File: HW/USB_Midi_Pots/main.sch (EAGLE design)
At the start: 61 parts, among them SW1 EC12E_SW

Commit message: HW update
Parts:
- added C20: (no value), Ai_Passives:CAP0805
- added USB2: (no value), pinhead:PINHD-1X4
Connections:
- net +5V: now also C20.1, USB2.4
- net GND: now also C20.2, USB2.1
- net N$1: now also USB2.3
- net N$2: now also USB2.2
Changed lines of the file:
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@@
 <setting verticaltext="up"/>
 </settings>
-<grid distance="0.05" unitdist="inch" unit="inch" style="lines" multiple="1" display="no" altdistance="0.01" altunitdist="inch" altunit="inch"/>
+<grid distance="0.1" unitdist="inch" unit="inch" style="lines" multiple="1" display="no" altdistance="0.01" altunitdist="inch" altunit="inch"/>
 <layers>
 <layer number="1" name="Top" color="4" fill="1" visible="no" active="no"/>
@@
 <layer number="113" name="IDFDebug" color="4" fill="1" visible="yes" active="yes"/>
 <layer number="116" name="Patch_BOT" color="9" fill="4" visible="no" active="yes"/>
+<layer number="117" name="mPads" color="7" fill="1" visible="no" active="no"/>
+<layer number="118" name="mVias" color="7" fill="1" visible="no" active="no"/>
+<layer number="119" name="mUnrouted" color="7" fill="1" visible="no" active="no"/>
+<layer number="120" name="mDimension" color="7" fill="1" visible="no" active="no"/>
 <layer number="121" name="_tsilk" color="7" fill="1" visible="no" active="yes"/>
 <layer number="122" name="_bsilk" color="7" fill="1" visible="no" active="yes"/>
@@
 <layer number="127" name="_tValues" color="7" fill="1" visible="yes" active="yes"/>
 <layer number="128" name="_bValues" color="7" fill="1" visible="yes" active="yes"/>
+<layer number="129" name="mtStop" color="7" fill="1" visible="no" active="no"/>
+<layer number="130" name="mbStop" color="7" fill="1" visible="no" active="no"/>
 <layer number="131" name="tAdjust" color="7" fill="1" visible="no" active="yes"/>
 <layer number="132" name="bAdjust" color="7" fill="1" visible="no" active="yes"/>
+<layer number="133" name="mtFinish" color="7" fill="1" visible="no" active="no"/>
+<layer number="134" name="mbFinish" color="7" fill="1" visible="no" active="no"/>
+<layer number="135" name="mtGlue" color="7" fill="1" visible="no" active="no"/>
+<layer number="136" name="mbGlue" color="7" fill="1" visible="no" active="no"/>
+<layer number="137" name="mtTest" color="7" fill="1" visible="no" active="no"/>
+<layer number="138" name="mbTest" color="7" fill="1" visible="no" active="no"/>
+<layer number="139" name="mtKeepout" color="7" fill="1" visible="no" active="no"/>
+<layer number="140" name="mbKeepout" color="7" fill="1" visible="no" active="no"/>
+<layer number="141" name="mtRestrict" color="7" fill="1" visible="no" active="no"/>
+<layer number="142" name="mbRestrict" color="7" fill="1" visible="no" active="no"/>
+<layer number="143" name="mvRestrict" color="7" fill="1" visible="no" active="no"/>
 <layer number="144" name="Drill_legend" color="7" fill="1" visible="no" active="yes"/>
+<layer number="145" name="mHoles" color="7" fill="1" visible="no" active="no"/>
+<layer number="146" name="mMilling" color="7" fill="1" visible="no" active="no"/>
+<layer number="147" name="mMeasures" color="7" fill="1" visible="no" active="no"/>
+<layer number="148" name="mDocument" color="7" fill="1" visible="no" active="no"/>
+<layer number="149" name="mReference" color="7" fill="1" visible="no" active="no"/>
 <layer number="150" name="Notes" color="7" fill="1" visible="no" active="yes"/>
 <layer number="151" name="HeatSink" color="7" fill="1" visible="no" active="yes"/>
@@
 <layer number="154" name="FabDoc2" color="2" fill="1" visible="no" active="no"/>
 <layer number="155" name="FabDoc3" color="7" fill="15" visible="no" active="no"/>
+<layer number="191" name="mNets" color="7" fill="1" visible="no" active="no"/>
+<layer number="192" name="mBusses" color="7" fill="1" visible="no" active="no"/>
+<layer number="193" name="mPins" color="7" fill="1" visible="no" active="no"/>
+<layer number="194" name="mSymbols" color="7" fill="1" visible="no" active="no"/>
+<layer number="195" name="mNames" color="7" fill="1" visible="no" active="no"/>
+<layer number="196" name="mValues" color="7" fill="1" visible="no" active="no"/>
 <layer number="199" name="Contour" color="7" fill="1" visible="no" active="yes"/>
 <layer number="200" name="200bmp" color="1" fill="10" visible="no" active="yes"/>
@@
 <part name="P+11" library="supply1" library_urn="urn:adsk.eagle:library:371" deviceset="+5V" device=""/>
 <part name="GND17" library="supply1" library_urn="urn:adsk.eagle:library:371" deviceset="GND" device=""/>
+<part name="C20" library="Ai_Passives" deviceset="CAP" device="0805"/>
+<part name="USB2" library="pinhead" library_urn="urn:adsk.eagle:library:325" deviceset="PINHD-1X4" device="" package3d_urn="urn:adsk.eagle:package:22407/2"/>
 </parts>
 <sheets>
@@
 <instance part="P+11" gate="1" x="110.49" y="33.02" rot="R90"/>
 <instance part="GND17" gate="1" x="110.49" y="40.64" rot="R270"/>
+<instance part="C20" gate="G$1" x="-5.08" y="233.68"/>
+<instance part="USB2" gate="A" x="-88.9" y="96.52" rot="R180"/>
 </instances>
 <busses>
@@
 <pinref part="C5" gate="G$1" pin="2"/>
 <wire x1="-12.7" y1="226.06" x2="-12.7" y2="228.6" width="0.1524" layer="91"/>
+<pinref part="C20" gate="G$1" pin="2"/>
+<wire x1="-5.08" y1="228.6" x2="-5.08" y2="226.06" width="0.1524" layer="91"/>
+<wire x1="-5.08" y1="226.06" x2="-12.7" y2="226.06" width="0.1524" layer="91"/>
+<junction x="-12.7" y="226.06"/>
 </segment>
 <segment>
@@
 <wire x1="-86.36" y1="38.1" x2="-83.82" y2="38.1" width="0.1524" layer="91"/>
 <junction x="-83.82" y="38.1"/>
+<wire x1="-68.58" y1="72.39" x2="-68.58" y2="71.12" width="0.1524" layer="91"/>
+<junction x="-68.58" y="48.26"/>
+<pinref part="USB2" gate="A" pin="1"/>
+<wire x1="-68.58" y1="71.12" x2="-68.58" y2="48.26" width="0.1524" layer="91"/>
+<wire x1="-86.36" y1="91.44" x2="-71.12" y2="91.44" width="0.1524" layer="91"/>
+<wire x1="-71.12" y1="91.44" x2="-68.58" y2="91.44" width="0.1524" layer="91"/>
+<wire x1="-68.58" y1="91.44" x2="-68.58" y2="71.12" width="0.1524" layer="91"/>
 </segment>
 <segment>
@@
 <wire x1="12.7" y1="50.8" x2="-21.59" y2="50.8" width="0.1524" layer="91"/>
 <wire x1="-21.59" y1="50.8" x2="-21.59" y2="58.42" width="0.1524" layer="91"/>
-<wire x1="-21.59" y1="58.42" x2="-73.66" y2="58.42" width="0.1524" layer="91"/>
+<wire x1="-21.59" y1="58.42" x2="-60.96" y2="58.42" width="0.1524" layer="91"/>
 <pinref part="P+5" gate="1" pin="+5V"/>
+<wire x1="-60.96" y1="58.42" x2="-73.66" y2="58.42" width="0.1524" layer="91"/>
 <wire x1="12.7" y1="53.34" x2="12.7" y2="50.8" width="0.1524" layer="91"/>
 <junction x="12.7" y="50.8"/>
 <pinref part="U$2" gate="G$1" pin="VCC"/>
+<wire x1="-60.96" y1="80.01" x2="-60.96" y2="78.74" width="0.1524" layer="91"/>
+<wire x1="-60.96" y1="78.74" x2="-60.96" y2="58.42" width="0.1524" layer="91"/>
+<junction x="-60.96" y="58.42"/>
+<pinref part="USB2" gate="A" pin="4"/>
+<wire x1="-86.36" y1="99.06" x2="-60.96" y2="99.06" width="0.1524" layer="91"/>
+<wire x1="-60.96" y1="99.06" x2="-60.96" y2="96.52" width="0.1524" layer="91"/>
+<wire x1="-60.96" y1="96.52" x2="-60.96" y2="78.74" width="0.1524" layer="91"/>
 </segment>
 <segment>
@@
 <wire x1="-20.32" y1="238.76" x2="-20.32" y2="241.3" width="0.1524" layer="91"/>
 <junction x="-20.32" y="241.3"/>
+<pinref part="C20" gate="G$1" pin="1"/>
+<wire x1="-5.08" y1="238.76" x2="-5.08" y2="241.3" width="0.1524" layer="91"/>
+<wire x1="-5.08" y1="241.3" x2="-12.7" y2="241.3" width="0.1524" layer="91"/>
+<junction x="-12.7" y="241.3"/>
 </segment>
 <segment>
@@
 <wire x1="-45.72" y1="46.99" x2="-45.72" y2="55.88" width="0.1524" layer="91"/>
 <junction x="-45.72" y="55.88"/>
-<wire x1="-73.66" y1="55.88" x2="-45.72" y2="55.88" width="0.1524" layer="91"/>
+<wire x1="-73.66" y1="55.88" x2="-63.5" y2="55.88" width="0.1524" layer="91"/>
 <pinref part="U$2" gate="G$1" pin="D-"/>
+<wire x1="-63.5" y1="55.88" x2="-45.72" y2="55.88" width="0.1524" layer="91"/>
+<wire x1="-63.5" y1="77.47" x2="-63.5" y2="76.2" width="0.1524" layer="91"/>
+<wire x1="-63.5" y1="76.2" x2="-63.5" y2="55.88" width="0.1524" layer="91"/>
+<junction x="-63.5" y="55.88"/>
+<pinref part="USB2" gate="A" pin="3"/>
+<wire x1="-86.36" y1="96.52" x2="-63.5" y2="96.52" width="0.1524" layer="91"/>
+<wire x1="-63.5" y1="96.52" x2="-63.5" y2="76.2" width="0.1524" layer="91"/>
 </segment>
 </net>
@@
 <wire x1="-40.64" y1="46.99" x2="-40.64" y2="53.34" width="0.1524" layer="91"/>
 <junction x="-40.64" y="53.34"/>
-<wire x1="-73.66" y1="53.34" x2="-40.64" y2="53.34" width="0.1524" layer="91"/>
+<wire x1="-73.66" y1="53.34" x2="-66.04" y2="53.34" width="0.1524" layer="91"/>
 <pinref part="U$2" gate="G$1" pin="D+"/>
+<wire x1="-66.04" y1="53.34" x2="-40.64" y2="53.34" width="0.1524" layer="91"/>
+<wire x1="-66.04" y1="74.93" x2="-66.04" y2="73.66" width="0.1524" layer="91"/>
+<wire x1="-66.04" y1="73.66" x2="-66.04" y2="53.34" width="0.1524" layer="91"/>
+<junction x="-66.04" y="53.34"/>
+<pinref part="USB2" gate="A" pin="2"/>
+<wire x1="-86.36" y1="93.98" x2="-66.04" y2="93.98" width="0.1524" layer="91"/>
+<wire x1="-66.04" y1="93.98" x2="-66.04" y2="73.66" width="0.1524" layer="91"/>
 </segment>
 </net>

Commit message: Board Update
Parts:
- added D7: (no value), Ai_LED:LED0603
- added L3: (no value), Ai_Passives:IND0603
- added R6: (no value), Ai_Passives:RES0603
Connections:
- new net N$36: R6.1, U$1.(INT6/AIN0)PE6
- new net N$38: D7.A, R6.2
- new net N$40: L3.1, U$2.VCC, USB2.4
- net +5V: now also L3.2; no longer U$2.VCC, USB2.4
- net GND: now also D7.C
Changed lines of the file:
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@@
 <setting verticaltext="up"/>
 </settings>
-<grid distance="0.1" unitdist="inch" unit="inch" style="lines" multiple="1" display="no" altdistance="0.01" altunitdist="inch" altunit="inch"/>
+<grid distance="0.05" unitdist="inch" unit="inch" style="lines" multiple="1" display="no" altdistance="0.01" altunitdist="inch" altunit="inch"/>
 <layers>
 <layer number="1" name="Top" color="4" fill="1" visible="no" active="no"/>
@@
 <part name="C20" library="Ai_Passives" deviceset="CAP" device="0805"/>
 <part name="USB2" library="pinhead" library_urn="urn:adsk.eagle:library:325" deviceset="PINHD-1X4" device="" package3d_urn="urn:adsk.eagle:package:22407/2"/>
+<part name="R6" library="Ai_Passives" deviceset="RES" device="0603"/>
+<part name="D7" library="Ai_LED" deviceset="LED" device="0603"/>
+<part name="L3" library="Ai_Passives" deviceset="IND" device="0603"/>
 </parts>
 <sheets>
@@
 <instance part="C20" gate="G$1" x="-5.08" y="233.68"/>
 <instance part="USB2" gate="A" x="-88.9" y="96.52" rot="R180"/>
+<instance part="R6" gate="G$1" x="92.71" y="58.42"/>
+<instance part="D7" gate="G$1" x="109.22" y="58.42" rot="R90"/>
+<instance part="L3" gate="G$1" x="-7.62" y="50.8" rot="R90"/>
 </instances>
 <busses>
@@
 <junction x="118.11" y="71.12"/>
 <pinref part="PIN8" gate="G$1" pin="C"/>
-<wire x1="114.3" y1="66.04" x2="118.11" y2="66.04" width="0.1524" layer="91"/>
+<wire x1="114.3" y1="66.04" x2="116.84" y2="66.04" width="0.1524" layer="91"/>
+<wire x1="116.84" y1="66.04" x2="118.11" y2="66.04" width="0.1524" layer="91"/>
 <wire x1="118.11" y1="66.04" x2="118.11" y2="68.58" width="0.1524" layer="91"/>
 <pinref part="PIN7" gate="G$1" pin="C"/>
@@
 <wire x1="107.95" y1="68.58" x2="118.11" y2="68.58" width="0.1524" layer="91"/>
 <junction x="118.11" y="68.58"/>
+<pinref part="D7" gate="G$1" pin="C"/>
+<wire x1="114.3" y1="58.42" x2="116.84" y2="58.42" width="0.1524" layer="91"/>
+<wire x1="116.84" y1="58.42" x2="116.84" y2="66.04" width="0.1524" layer="91"/>
+<junction x="116.84" y="66.04"/>
 </segment>
 <segment>
@@
 <wire x1="21.59" y1="60.96" x2="21.59" y2="50.8" width="0.1524" layer="91"/>
 <wire x1="21.59" y1="50.8" x2="12.7" y2="50.8" width="0.1524" layer="91"/>
-<wire x1="12.7" y1="50.8" x2="-21.59" y2="50.8" width="0.1524" layer="91"/>
-<wire x1="-21.59" y1="50.8" x2="-21.59" y2="58.42" width="0.1524" layer="91"/>
-<wire x1="-21.59" y1="58.42" x2="-60.96" y2="58.42" width="0.1524" layer="91"/>
 <pinref part="P+5" gate="1" pin="+5V"/>
-<wire x1="-60.96" y1="58.42" x2="-73.66" y2="58.42" width="0.1524" layer="91"/>
 <wire x1="12.7" y1="53.34" x2="12.7" y2="50.8" width="0.1524" layer="91"/>
+<pinref part="L3" gate="G$1" pin="2"/>
+<wire x1="-2.54" y1="50.8" x2="12.7" y2="50.8" width="0.1524" layer="91"/>
 <junction x="12.7" y="50.8"/>
-<pinref part="U$2" gate="G$1" pin="VCC"/>
-<wire x1="-60.96" y1="80.01" x2="-60.96" y2="78.74" width="0.1524" layer="91"/>
-<wire x1="-60.96" y1="78.74" x2="-60.96" y2="58.42" width="0.1524" layer="91"/>
-<junction x="-60.96" y="58.42"/>
-<pinref part="USB2" gate="A" pin="4"/>
-<wire x1="-86.36" y1="99.06" x2="-60.96" y2="99.06" width="0.1524" layer="91"/>
-<wire x1="-60.96" y1="99.06" x2="-60.96" y2="96.52" width="0.1524" layer="91"/>
-<wire x1="-60.96" y1="96.52" x2="-60.96" y2="78.74" width="0.1524" layer="91"/>
 </segment>
 <segment>
@@
 </segment>
 </net>
+<net name="N$36" class="0">
+<segment>
+<pinref part="U$1" gate="G$1" pin="(INT6/AIN0)PE6"/>
+<pinref part="R6" gate="G$1" pin="1"/>
+<wire x1="83.82" y1="58.42" x2="87.63" y2="58.42" width="0.1524" layer="91"/>
+</segment>
+</net>
+<net name="N$38" class="0">
+<segment>
+<pinref part="R6" gate="G$1" pin="2"/>
+<pinref part="D7" gate="G$1" pin="A"/>
+<wire x1="97.79" y1="58.42" x2="106.68" y2="58.42" width="0.1524" layer="91"/>
+</segment>
+</net>
+<net name="N$40" class="0">
+<segment>
+<pinref part="L3" gate="G$1" pin="1"/>
+<wire x1="-21.59" y1="50.8" x2="-12.7" y2="50.8" width="0.1524" layer="91"/>
+<wire x1="-21.59" y1="50.8" x2="-21.59" y2="58.42" width="0.1524" layer="91"/>
+<wire x1="-21.59" y1="58.42" x2="-60.96" y2="58.42" width="0.1524" layer="91"/>
+<wire x1="-60.96" y1="58.42" x2="-73.66" y2="58.42" width="0.1524" layer="91"/>
+<pinref part="U$2" gate="G$1" pin="VCC"/>
+<wire x1="-60.96" y1="99.06" x2="-60.96" y2="58.42" width="0.1524" layer="91"/>
+<junction x="-60.96" y="58.42"/>
+<pinref part="USB2" gate="A" pin="4"/>
+<wire x1="-86.36" y1="99.06" x2="-60.96" y2="99.06" width="0.1524" layer="91"/>
+</segment>
+</net>

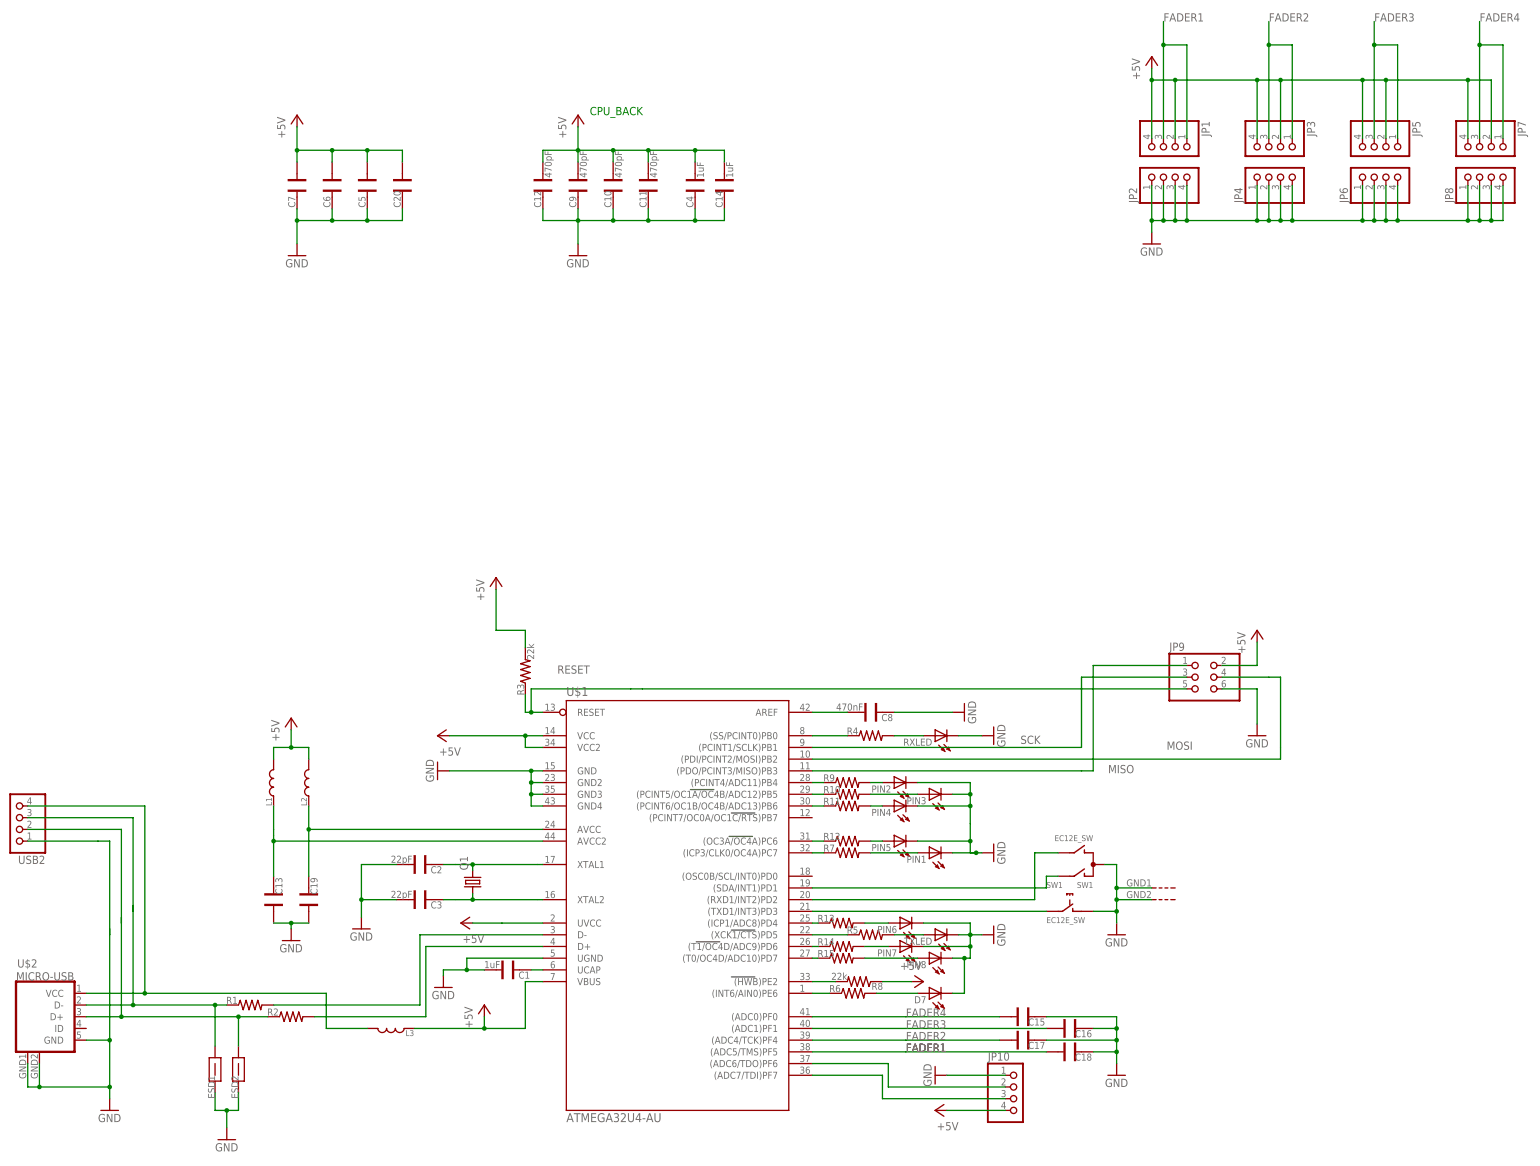
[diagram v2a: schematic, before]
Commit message: Rotary Encoder Test and other Board Layouts
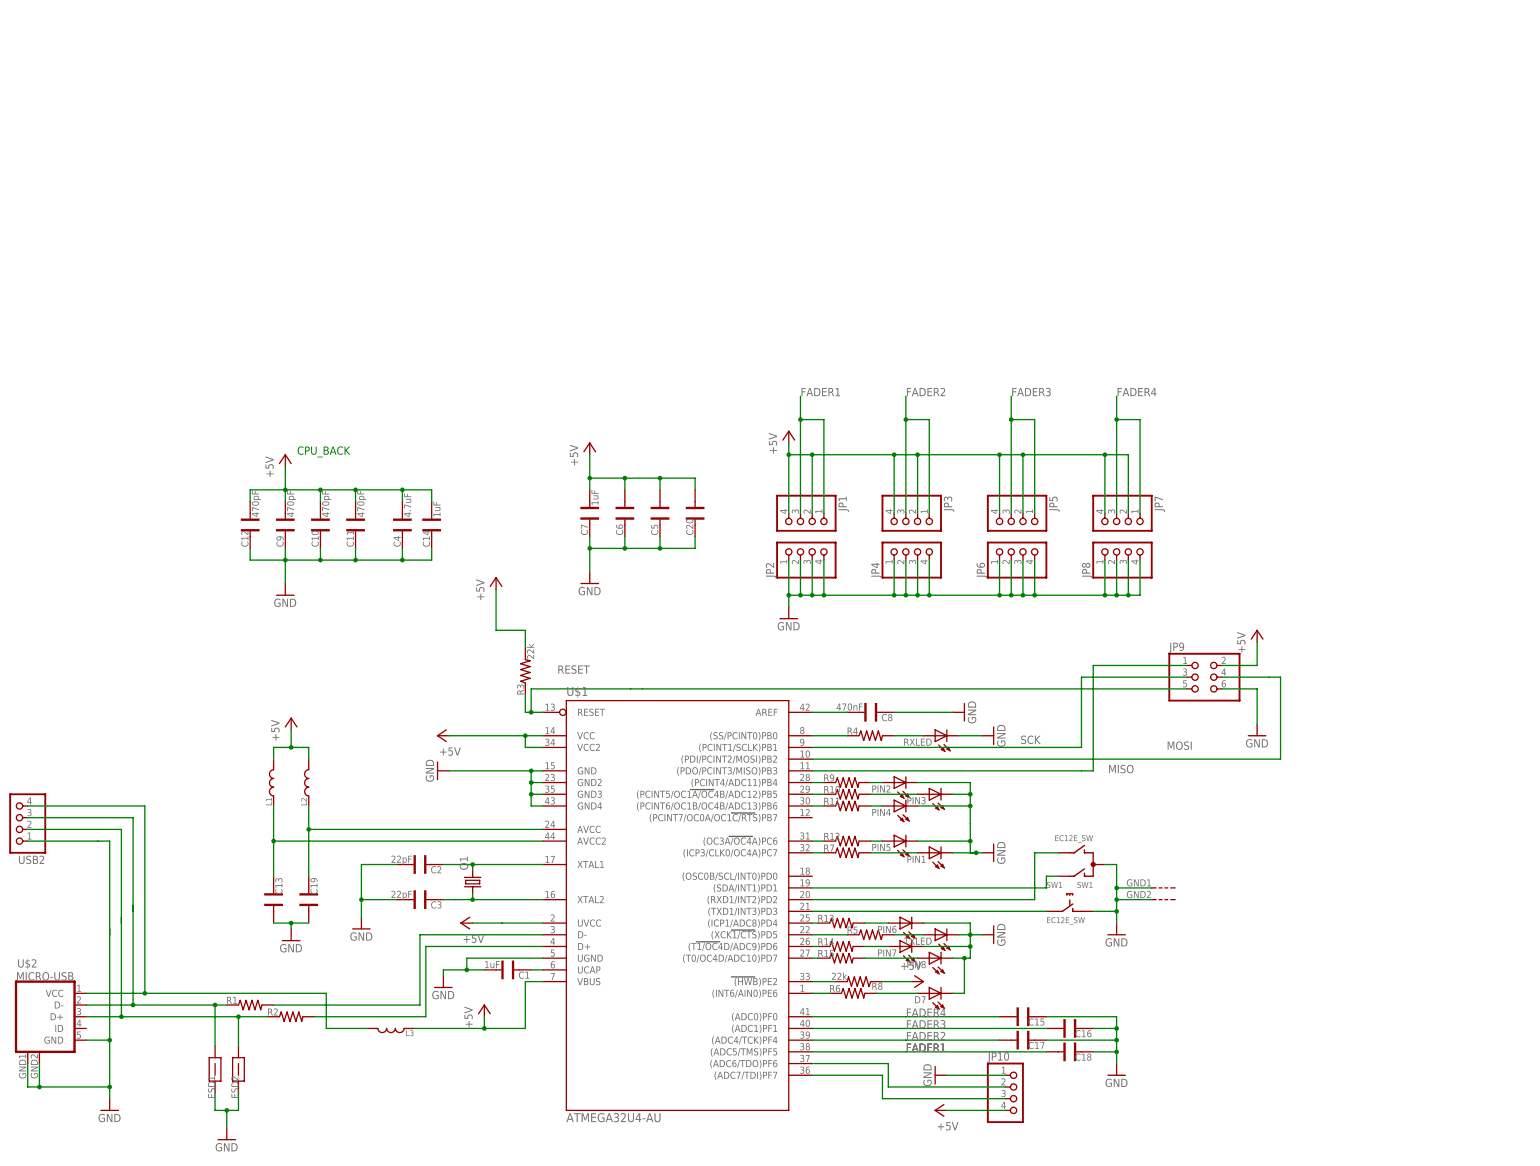
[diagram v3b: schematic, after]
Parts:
- C4: value 1uF -> 4.7uF
- C7: value (none) -> 1uF
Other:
- moved on the sheet: C10, C11, C12, C14, C20, C4, C5, C6, C7, C9, JP1, JP2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
